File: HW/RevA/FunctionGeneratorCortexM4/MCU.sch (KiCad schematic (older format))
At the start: 12 parts

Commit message: hw update
- Added MCU section
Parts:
- removed R? (x3): 50R, symbol Device:R
- added J?: Conn_02x04_Odd_Even, symbol Connector_Generic:Conn_02x04_Odd_Even
- added J? (x2): Conn_01x03, symbol Connector_Generic:Conn_01x03
- added JP? (x10): Jumper_NC_Small, Jumper:SolderJumper-2_P1.3mm_Bridged_Pad1.0x1.5mm, symbol Device:Jumper_NC_Small
- added R? (x4): 220R, symbol Device:R
- added U? (x4): Tactile_Switch_SPST-NO, symbol Tactile_SPST-NO:Tactile_Switch_SPST-NO
- added U? (x2): 74LVC1G3157, symbol 74xGxx:74LVC1G3157
- JP? (x3): footprint (none) -> Jumper:SolderJumper-2_P1.3mm_Bridged_Pad1.0x1.5mm
- JP?: footprint (none) -> Connector_PinHeader_2.54mm:PinHeader_1x02_P2.54mm_Vertical
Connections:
- net labels added: 3V3_VIN, ADC_IN1, ADC_IN2, AUX_PRE, BTN1, BTN2, BTN3, BTN4, CH1_MUX, CH2_MUX, COMP1_INP, COMP2_INP, DAC1_OUT1, DAC1_OUT2, DAC2_OUT1, ENC_A, ENC_B, FUNC1_PRE, FUNC2_PRE, TFT_CS, TFT_DC, TFT_GND, TFT_LED, TFT_MOSI, TFT_RST, TFT_SCK, TFT_VCC, TIM1_TF1FP1, TIM2_TF2FP2
- net labels removed: 5V, AUX_OUT, FUNC1_OUT, FUNC2_OUT
- wire segments 33 -> 131
- no-connect marks 0 -> 9
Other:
- note added: "Internal VREF"
- note added: "TIM4_CH1"
- note added: "TIM4_CH2"
- moved on the sheet: JP?, R?, SW?, U?A

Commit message: Finished Schema
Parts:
- removed J?: Conn_01x03, symbol Connector_Generic:Conn_01x03
- removed R? (x6): 220R, symbol Device:R
- removed SW?: Rotary_Encoder_Switch, symbol Device:Rotary_Encoder_Switch
- removed U? (x4): Tactile_Switch_SPST-NO, symbol Tactile_SPST-NO:Tactile_Switch_SPST-NO
- removed U?: 74LVC1G3157, symbol 74xGxx:74LVC1G3157
- added J3: Conn_02x06_Odd_Even, Connector_IDC:IDC-Header_2x06_P2.54mm_Vertical, symbol Connector_Generic:Conn_02x06_Odd_Even
- added J4: Conn_01x06, Connector_PinHeader_2.54mm:PinHeader_1x06_P2.54mm_Vertical, symbol Connector_Generic:Conn_01x06
- added J7: Conn_02x07_Odd_Even, Connector_PinHeader_1.27mm:PinHeader_2x07_P1.27mm_Vertical_SMD, symbol Connector_Generic:Conn_02x07_Odd_Even
- added R11: 100R, Resistor_SMD:R_1206_3216Metric_Pad1.42x1.75mm_HandSolder, symbol Device:R
- J5: renamed from J?; footprint (none) -> Connector_PinHeader_1.27mm:PinHeader_1x03_P1.27mm_Vertical
- J6: renamed from J?; footprint (none) -> Connector_IDC:IDC-Header_2x04_P2.54mm_Vertical
- R7: renamed from R?; footprint (none) -> Resistor_SMD:R_1206_3216Metric_Pad1.42x1.75mm_HandSolder
- U2: renamed from U?; footprint (none) -> Package_TO_SOT_SMD:SC-70-8_Handsoldering
- gave numbers to parts that had none: 15
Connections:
- net BTN1: now also J3.4 (Pin_4)
- net BTN2: now also J3.6 (Pin_6)
- net BTN3: now also J3.8 (Pin_8)
- net BTN4: now also J3.10 (Pin_10)
- net ENC_A: now also J3.3 (Pin_3)
- net ENC_B: now also J3.5 (Pin_5)
- net ENC_SW: now also U6.39 (PC7), J3.9 (Pin_9)
- net GND: now also J6.2 (Pin_2), J3.11 (Pin_11), J3.12 (Pin_12), J3.7 (Pin_7), J4.3 (Pin_3), J7.5 (Pin_5), J7.7 (Pin_7), R11.2; no longer J6.4 (Pin_4)
- net TFT_CS: now also J6.3 (Pin_3); no longer J6.6 (Pin_6)
- net TFT_DC: now also J6.5 (Pin_5); no longer J6.7 (Pin_7)
- net TFT_MOSI: now also J6.6 (Pin_6); no longer J6.5 (Pin_5)
- net TFT_RST: now also J6.4 (Pin_4); no longer J6.8 (Pin_8)
- net TFT_SCK: now also J6.7 (Pin_7); no longer J6.3 (Pin_3)
- net T_NRST: now also J4.5 (Pin_5), J7.12 (Pin_12)
- net T_SWCLK: now also J4.2 (Pin_2), J7.6 (Pin_6)
- net T_SWDIO: now also J4.4 (Pin_4), J7.4 (Pin_4)
- net T_SWO: now also J4.6 (Pin_6), J7.8 (Pin_8)
- net VCC: now also J6.8 (Pin_8), J3.1 (Pin_1), J3.2 (Pin_2), J4.1 (Pin_1), J7.3 (Pin_3); no longer J6.2 (Pin_2)
- net SG0_OUT: now reaches U6.22 (PC4)
- net SG1_OUT: now reaches U6.23 (PC5)
- net SG2_OUT: now reaches U6.38 (PC6)
- net ADC_IN2: no longer names the net of U6.13 (PA1)
- net AUX_PRE renamed FUNC1_SYNC
- net CH2_MUX renamed DCBIAS_INVERT_OUT
- net COMP2_INP: no longer names the net of U6.17 (PA3)
- net FUNC1_PRE renamed FUNC1_SIG
- net FUNC2_PRE renamed FUNC1_DCBIAS
- net TIM2_TF2FP2: no longer names the net of U6.51 (PA15)
- new net: J7.11 (Pin_11), R11.1
- no-connect marks 9 -> 30
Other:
- note added: "6-pin SWD ICP Connector"
- note added: "Control Front Panel Connector\nRotEncoder and Tactile SPST"
- note added: "MIPI10/STDC14 ICP Connector"
- note added: "TFT Front Panel Display Connector"
- note added: "Using Internal VREF"
- note removed: "Internal VREF"
- moved on the sheet: J5, J6, JP1, JP10, JP11, JP12, JP13, JP14, JP2, JP3, JP4, JP5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

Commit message: Completed RevA layout
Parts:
- removed JP1, JP11, JP12, JP13, JP14, JP2, JP3, JP4, JP5, JP6, JP7, JP8, JP9: Jumper_NC_Small, Jumper:SolderJumper-2_P1.3mm_Bridged_Pad1.0x1.5mm, symbol Device:Jumper_NC_Small
- removed U2: 74LVC1G3157, Package_TO_SOT_SMD:SC-70-8_Handsoldering, symbol 74xGxx:74LVC1G3157
- added U2: SN74LVC1G3157DCKR, Package_TO_SOT_SMD:SOT-363_SC-70-6_Handsoldering, symbol SN74LVC1G3157:SN74LVC1G3157DCKR
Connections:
- net CH1_MUX: now also U2.6 (S)
- net ENC_A: now also U6.45 (PA11)
- net ENC_B: now also U6.46 (PA12)
- net FUNC1_DCBIAS: now also U6.19 (PA5)
- net FUNC1_SIG: now also U6.18 (PA4)
- net FUNC1_SYNC: now also U6.20 (PA6)
- net TFT_CS: now also U6.60 (PB7)
- net TFT_DC: now also U6.59 (PB6)
- net TFT_MOSI: now also U6.54 (PC12)
- net TFT_RST: now also U6.62 (PB9)
- net TFT_SCK: now also U6.52 (PC10)
- net TIM1_TF1FP1: now also U2.1 (B2)
- net TRIG_IN: now also U2.4 (A)
- net T_SWCLK: now also U6.50 (PA14)
- net T_SWDIO: now also U6.49 (PA13)
- net T_SWO: now also U6.56 (PB3)
- net at J5.1 (Pin_1): now also U2.3 (B1)
- net GND renamed GNDS
- net GNDS: now also U2.2 (GND)
- net VCC renamed 3V3_VIN
- net 3V3_VIN: now also U2.5 (VCC)

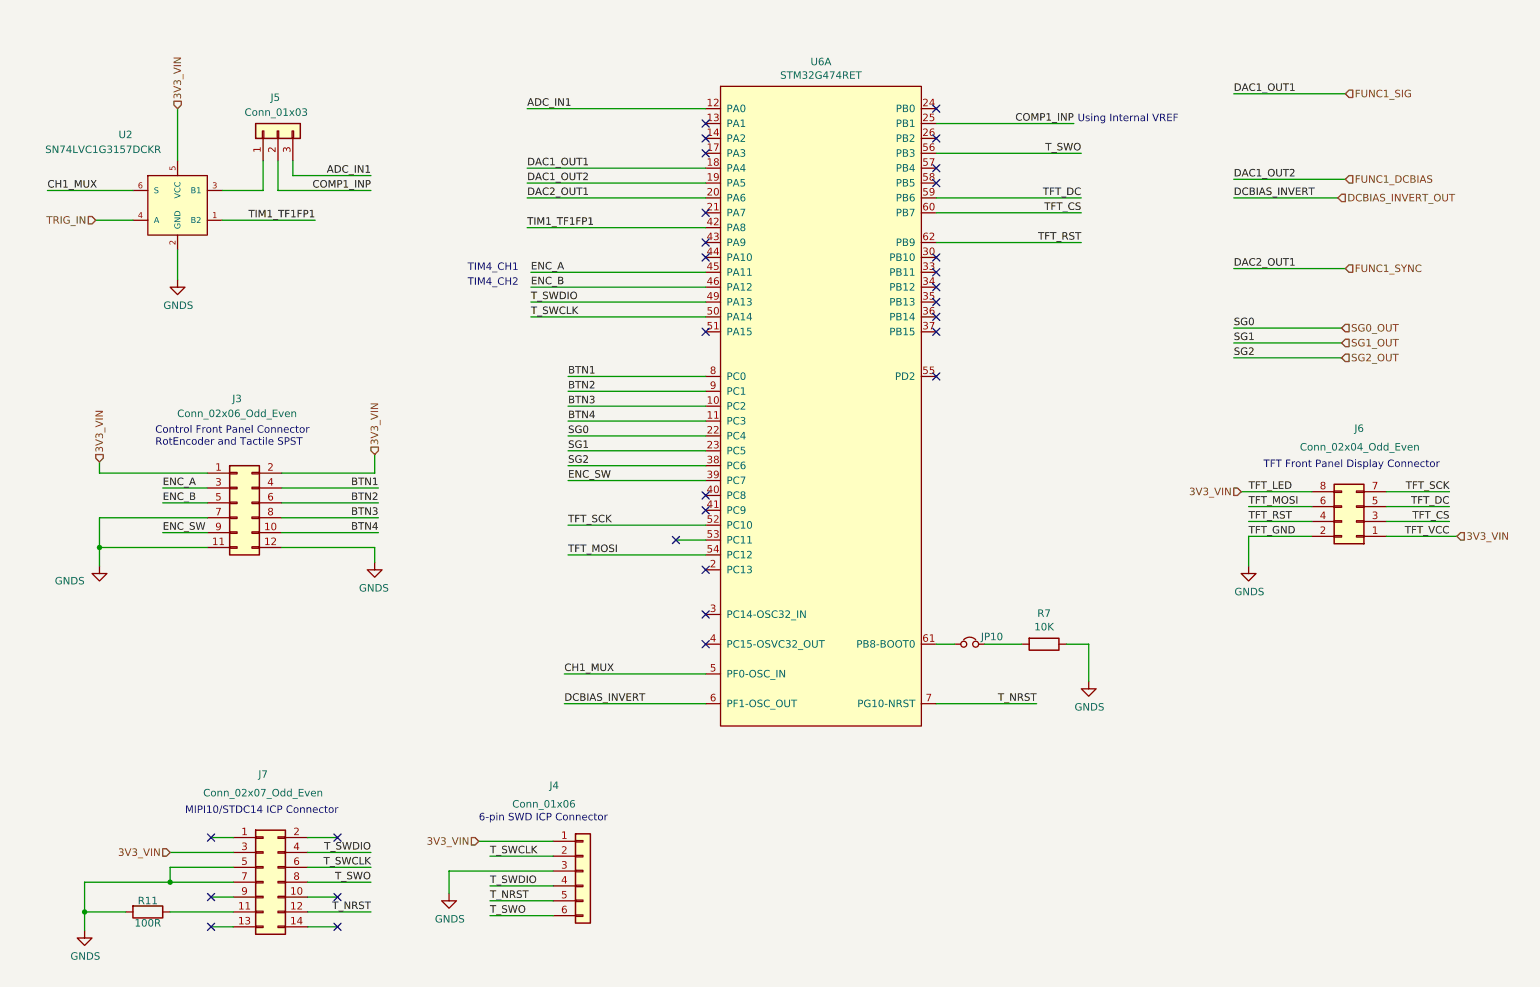
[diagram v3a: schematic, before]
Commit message: Finished RevA Layout
Dummy STMCubeMX project included in SW dir
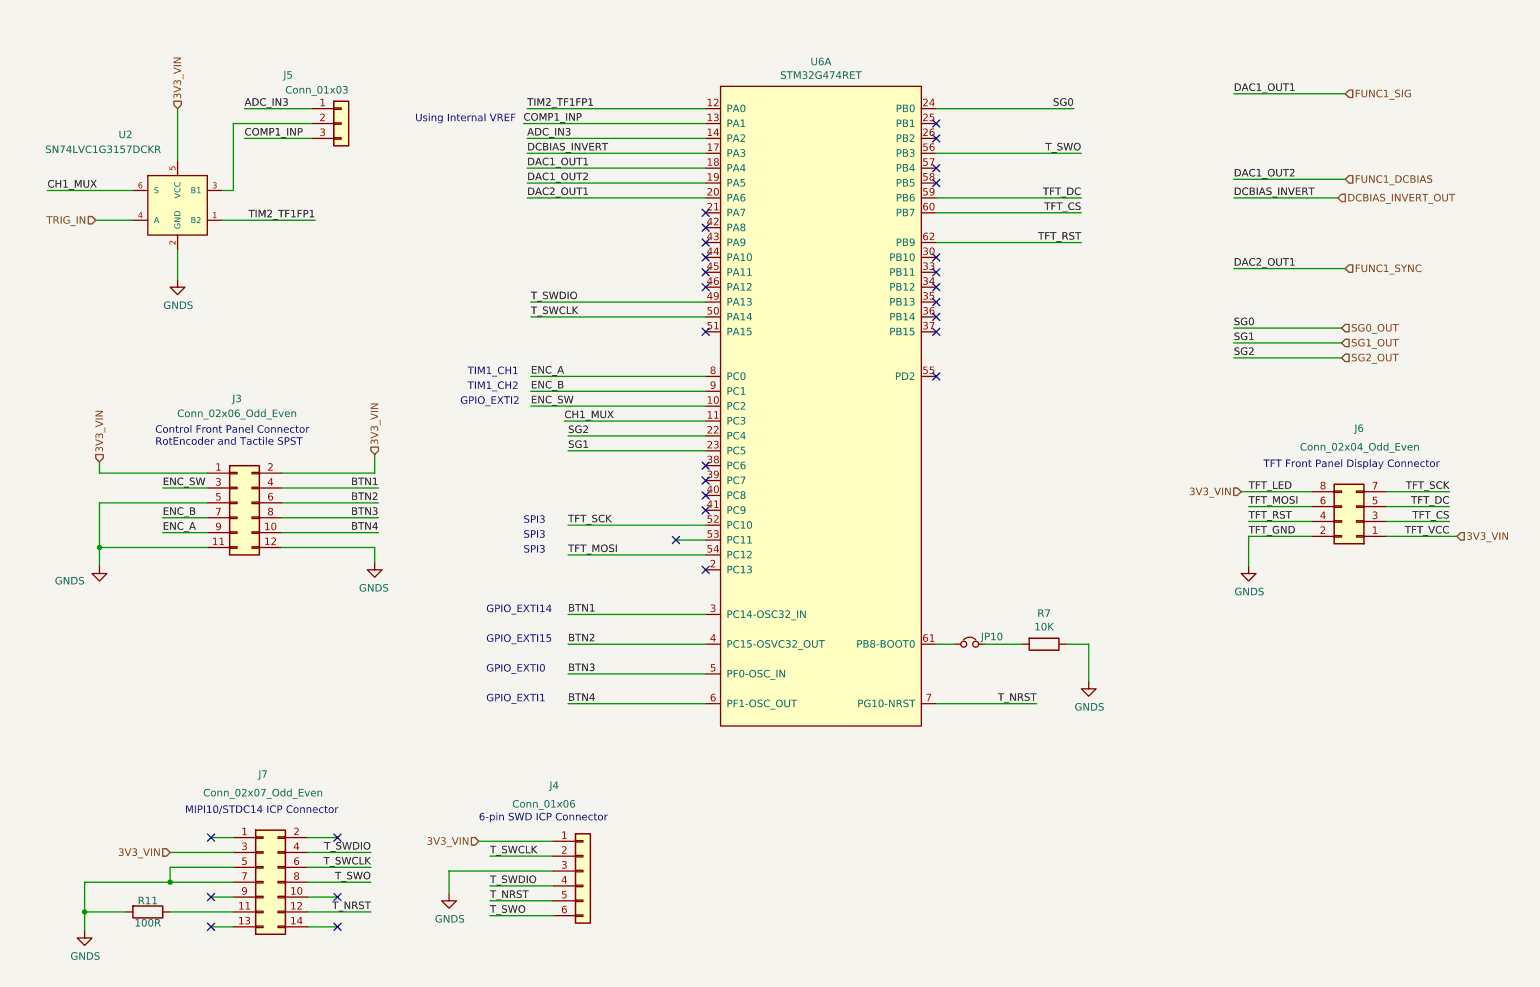
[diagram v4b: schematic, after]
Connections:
- net BTN1: now also U6.3 (PC14-OSC32_IN); no longer U6.8 (PC0)
- net BTN2: now also U6.4 (PC15-OSVC32_OUT); no longer U6.9 (PC1)
- net BTN3: now also U6.5 (PF0-OSC_IN); no longer U6.10 (PC2)
- net BTN4: now also U6.6 (PF1-OSC_OUT); no longer U6.11 (PC3)
- net CH1_MUX: now also U6.11 (PC3); no longer U6.5 (PF0-OSC_IN)
- net COMP1_INP: now also J5.3 (Pin_3), U6.13 (PA1); no longer J5.2 (Pin_2), U6.25 (PB1)
- net DCBIAS_INVERT_OUT: now also U6.17 (PA3); no longer U6.6 (PF1-OSC_OUT)
- net ENC_A: now also J3.9 (Pin_9), U6.8 (PC0); no longer J3.3 (Pin_3), U6.45 (PA11)
- net ENC_B: now also J3.7 (Pin_7), U6.9 (PC1); no longer J3.5 (Pin_5), U6.46 (PA12)
- net ENC_SW: now also J3.3 (Pin_3), U6.10 (PC2); no longer J3.9 (Pin_9), U6.39 (PC7)
- net GNDS: now also J3.5 (Pin_5); no longer J3.7 (Pin_7)
- net SG0_OUT: now also U6.24 (PB0); no longer U6.22 (PC4)
- net SG2_OUT: now also U6.22 (PC4); no longer U6.38 (PC6)
- net ADC_IN3: now reaches U6.14 (PA2)
- net ADC_IN3: now also J5.1 (Pin_1)
- net at U2.3 (B1): now also J5.2 (Pin_2); no longer J5.1 (Pin_1)
- net ADC_IN1 renamed TIM2_TF1FP1
- net TIM2_TF1FP1: now also U2.1 (B2); no longer J5.3 (Pin_3)
- net TIM1_TF1FP1: no longer names the net of U6.42 (PA8)
- net TIM1_TF1FP1: no longer U2.1 (B2)
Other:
- note added: "GPIO_EXTI0"
- note added: "GPIO_EXTI1"
- note added: "GPIO_EXTI14"
- note added: "GPIO_EXTI15"
- note added: "GPIO_EXTI2"
- note added: "SPI3"
- note added: "TIM1_CH1"
- note added: "TIM1_CH2"
- note removed: "TIM4_CH1"
- note removed: "TIM4_CH2"
- moved on the sheet: J5
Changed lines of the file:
@@
 Text HLabel 9750 2725 2    50   Input ~ 0
 FUNC1_SYNC
-Text Label 4275 2850 0    50   ~ 0
+Text Label 4275 3550 0    50   ~ 0
 ENC_B
-Text Label 4275 2750 0    50   ~ 0
+Text Label 4275 3450 0    50   ~ 0
 ENC_A
 Text Label 9100 4225 0    50   ~ 0
@@
 Wire Wire Line
 	9050 4225 9525 4225
-Text Notes 3850 2750 0    50   ~ 0
-TIM4_CH1
-Text Notes 3850 2850 0    50   ~ 0
-TIM4_CH2
-Text Label 4525 3450 0    50   ~ 0
+Text Notes 3850 3450 0    50   ~ 0
+TIM1_CH1
+Text Notes 3850 3550 0    50   ~ 0
+TIM1_CH2
+Text Label 4525 5050 0    50   ~ 0
 BTN1
-Text Label 4525 3550 0    50   ~ 0
+Text Label 4525 5250 0    50   ~ 0
 BTN2
-Text Label 4525 3650 0    50   ~ 0
+Text Label 4525 5450 0    50   ~ 0
 BTN3
-Text Label 4525 3750 0    50   ~ 0
+Text Label 4525 5650 0    50   ~ 0
 BTN4
 Text Label 4250 2050 0    50   ~ 0
@@
 Wire Wire Line
 	9000 2725 9750 2725
-Text Label 4250 2450 0    50   ~ 0
-TIM1_TF1FP1
 Text Label 4250 1650 0    50   ~ 0
-ADC_IN1
-Text Label 7925 1750 2    50   ~ 0
+TIM2_TF1FP1
+Text Label 4250 1850 0    50   ~ 0
+ADC_IN3
+Text Label 4225 1750 0    50   ~ 0
 COMP1_INP
 Text Label 2825 2400 2    50   ~ 0
-TIM1_TF1FP1
-Text Label 3200 2200 2    50   ~ 0
-COMP1_INP
-Text Label 3200 2100 2    50   ~ 0
-ADC_IN1
+TIM2_TF1FP1
 Wire Wire Line
 	2200 2400 2825 2400
@@
 Text Label 1025 2200 0    50   ~ 0
 CH1_MUX
-$Comp
-L Connector_Generic:Conn_01x03 J5
-U 1 1 5EDBA649
-P 2575 1800
-F 0 "J5" V 2800 1850 50  0000 R CNN
-F 1 "Conn_01x03" V 2700 2025 50  0000 R CNN
-F 2 "Connector_PinHeader_1.27mm:PinHeader_1x03_P1.27mm_Vertical" H 2575 1800 50  0001 C CNN
-F 3 "~" H 2575 1800 50  0001 C CNN
-	1    2575 1800
-	0    -1   -1   0
-$EndComp
-Wire Wire Line
-	2200 2200 2475 2200
-Wire Wire Line
-	2475 2200 2475 2000
-Wire Wire Line
-	2575 2000 2575 2200
-Wire Wire Line
-	2575 2200 3200 2200
-Wire Wire Line
-	2675 2100 2675 2000
-Wire Wire Line
-	2675 2100 3200 2100
-Text Label 4500 5450 0    50   ~ 0
-CH1_MUX
-Text Notes 7950 1750 0    50   ~ 0
+Text Notes 4175 1750 2    50   ~ 0
 Using Internal VREF
-Text Label 4500 5650 0    50   ~ 0
-DCBIAS_INVERT
 Wire Wire Line
 	9700 2250 9000 2250
@@
 Text HLabel 9700 2250 2    50   Input ~ 0
 DCBIAS_INVERT_OUT
-Text Label 4525 3850 0    50   ~ 0
+Text Label 7925 1650 2    50   ~ 0
 SG0
 Text Label 4525 3950 0    50   ~ 0
 SG1
-Text Label 4525 4050 0    50   ~ 0
+Text Label 4525 3850 0    50   ~ 0
 SG2
 Text HLabel 9725 3125 2    50   Input ~ 0
 SG0_OUT
-NoConn ~ 5450 1750
-NoConn ~ 5450 1850
-NoConn ~ 5450 1950
 NoConn ~ 5450 2350
 NoConn ~ 5450 2550
@@
 NoConn ~ 5450 4350
 NoConn ~ 5450 4750
-NoConn ~ 5450 5050
-NoConn ~ 5450 5250
 NoConn ~ 7000 3450
 NoConn ~ 7000 3150
@@
 NoConn ~ 7000 2050
 NoConn ~ 7000 1850
-NoConn ~ 7000 1650
+NoConn ~ 7000 1750
 $Comp
 L Connector_Generic:Conn_02x07_Odd_Even J7
@@
 Wire Wire Line
 	9000 3325 9725 3325
-Text Label 4525 4150 0    50   ~ 0
+Text Label 4275 3650 0    50   ~ 0
 ENC_SW
 Wire Wire Line
@@
 Text HLabel 9750 1550 2    50   Input ~ 0
 FUNC1_SIG
-Text Label 1800 4200 0    50   ~ 0
+Text Label 1800 4500 0    50   ~ 0
 ENC_A
 Wire Wire Line
-	2100 4200 1800 4200
-Wire Wire Line
-	2100 4300 1800 4300
-Text Label 1800 4300 0    50   ~ 0
+	2100 4500 1800 4500
+Wire Wire Line
+	2100 4400 1800 4400
+Text Label 1800 4400 0    50   ~ 0
 ENC_B
 Wire Wire Line
@@
 Text HLabel 1375 4025 1    50   Input ~ 0
 3V3_VIN
-Text Label 1800 4500 0    50   ~ 0
+Text Label 1800 4200 0    50   ~ 0
 ENC_SW
 Wire Wire Line
-	1800 4500 2100 4500
+	1800 4200 2100 4200
 Wire Wire Line
 	2600 4200 3250 4200
@@
 	1    0    0    -1
 $EndComp
-Wire Wire Line
-	2100 4400 1375 4400
-Wire Wire Line
-	1375 4400 1375 4600
 Connection ~ 1375 4600
 Wire Wire Line
@@
 	1350 2400 1600 2400
 Wire Wire Line
+	4525 4650 5450 4650
+Wire Wire Line
+	4525 4450 5450 4450
+Wire Wire Line
+	4275 3650 5450 3650
+Wire Wire Line
+	4525 3850 5450 3850
+Wire Wire Line
+	4525 3950 5450 3950
+Wire Wire Line
+	4525 5050 5450 5050
+Wire Wire Line
+	4525 5250 5450 5250
+Wire Wire Line
+	4525 5450 5450 5450
+Wire Wire Line
+	4525 5650 5450 5650
+Wire Wire Line
+	7925 1650 7000 1650
+Wire Wire Line
+	4275 3050 5450 3050
+Wire Wire Line
+	4275 2950 5450 2950
+Wire Wire Line
+	4275 3550 5450 3550
+Wire Wire Line
+	4275 3450 5450 3450
+Wire Wire Line
+	4250 2250 5450 2250
+Wire Wire Line
+	4250 2150 5450 2150
+Wire Wire Line
+	4250 2050 5450 2050
+Wire Wire Line
+	4250 1850 5450 1850
+Wire Wire Line
+	5450 1750 4225 1750
+Wire Wire Line
+	7000 1950 7975 1950
+Wire Wire Line
+	7000 2250 7975 2250
+Wire Wire Line
+	7000 2350 7975 2350
+Wire Wire Line
+	7000 2550 7975 2550
+Wire Wire Line
+	9000 1550 9750 1550
+Text Notes 3800 3650 0    50   ~ 0
+GPIO_EXTI2
+Wire Wire Line
+	1375 4300 2100 4300
+Wire Wire Line
+	1375 4300 1375 4600
+Text Notes 3975 5050 0    50   ~ 0
+GPIO_EXTI14
+Text Notes 3975 5250 0    50   ~ 0
+GPIO_EXTI15
+Text Notes 3975 5450 0    50   ~ 0
+GPIO_EXTI0
+Text Notes 3975 5650 0    50   ~ 0
+GPIO_EXTI1
+Wire Wire Line
+	2350 1850 2800 1850
+Wire Wire Line
+	2350 1650 2800 1650
+Wire Wire Line
 	1900 1650 1900 2000
 Wire Wire Line
-	4500 5450 5450 5450
-Wire Wire Line
-	4500 5650 5450 5650
-Wire Wire Line
-	4525 4650 5450 4650
-Wire Wire Line
-	4525 4450 5450 4450
-Wire Wire Line
-	4525 4150 5450 4150
-Wire Wire Line
-	4525 4050 5450 4050
-Wire Wire Line
-	4525 3950 5450 3950
-Wire Wire Line
-	4525 3450 5450 3450
-Wire Wire Line
-	4525 3550 5450 3550
-Wire Wire Line
-	4525 3650 5450 3650
-Wire Wire Line
-	4525 3750 5450 3750
-Wire Wire Line
-	4525 3850 5450 3850
-Wire Wire Line
-	4275 3050 5450 3050
-Wire Wire Line
-	4275 2950 5450 2950
-Wire Wire Line
-	4275 2850 5450 2850
-Wire Wire Line
-	4275 2750 5450 2750
-Wire Wire Line
-	4250 2450 5450 2450
-Wire Wire Line
-	4250 2250 5450 2250
-Wire Wire Line
-	4250 2150 5450 2150
-Wire Wire Line
-	4250 2050 5450 2050
+	2200 2200 2275 2200
+Wire Wire Line
+	2275 2200 2275 1750
+Wire Wire Line
+	2275 1750 2800 1750
 Wire Wire Line
 	4250 1650 5450 1650
 Wire Wire Line
-	7000 1750 7925 1750
-Wire Wire Line
-	7000 1950 7975 1950
-Wire Wire Line
-	7000 2250 7975 2250
-Wire Wire Line
-	7000 2350 7975 2350
-Wire Wire Line
-	7000 2550 7975 2550
-Wire Wire Line
-	9000 1550 9750 1550
+	4250 1950 5450 1950
+Text Label 4250 1950 0    50   ~ 0
+DCBIAS_INVERT
+Text Label 4500 3750 0    50   ~ 0
+CH1_MUX
+Wire Wire Line
+	4500 3750 5450 3750
+Text Notes 4225 4450 0    50   ~ 0
+SPI3
+Text Notes 4225 4650 0    50   ~ 0
+SPI3
+Text Notes 4225 4550 0    50   ~ 0
+SPI3
+NoConn ~ 5450 4050
+NoConn ~ 5450 4150
+NoConn ~ 5450 2750
+NoConn ~ 5450 2850
+NoConn ~ 5450 2450
+Text Label 2350 1650 0    50   ~ 0
+ADC_IN3
+Text Label 2350 1850 0    50   ~ 0
+COMP1_INP
+$Comp
+L Connector_Generic:Conn_01x03 J5
+U 1 1 5EDBA649
+P 3000 1750
+F 0 "J5" H 2675 2075 50  0000 R CNN
+F 1 "Conn_01x03" H 3050 1975 50  0000 R CNN
+F 2 "Connector_PinHeader_1.27mm:PinHeader_1x03_P1.27mm_Vertical" H 3000 1750 50  0001 C CNN
+F 3 "~" H 3000 1750 50  0001 C CNN
+	1    3000 1750
+	1    0    0    -1
+$EndComp
 $EndSCHEMATC
